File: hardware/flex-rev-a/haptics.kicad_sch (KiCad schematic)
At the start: 0 parts

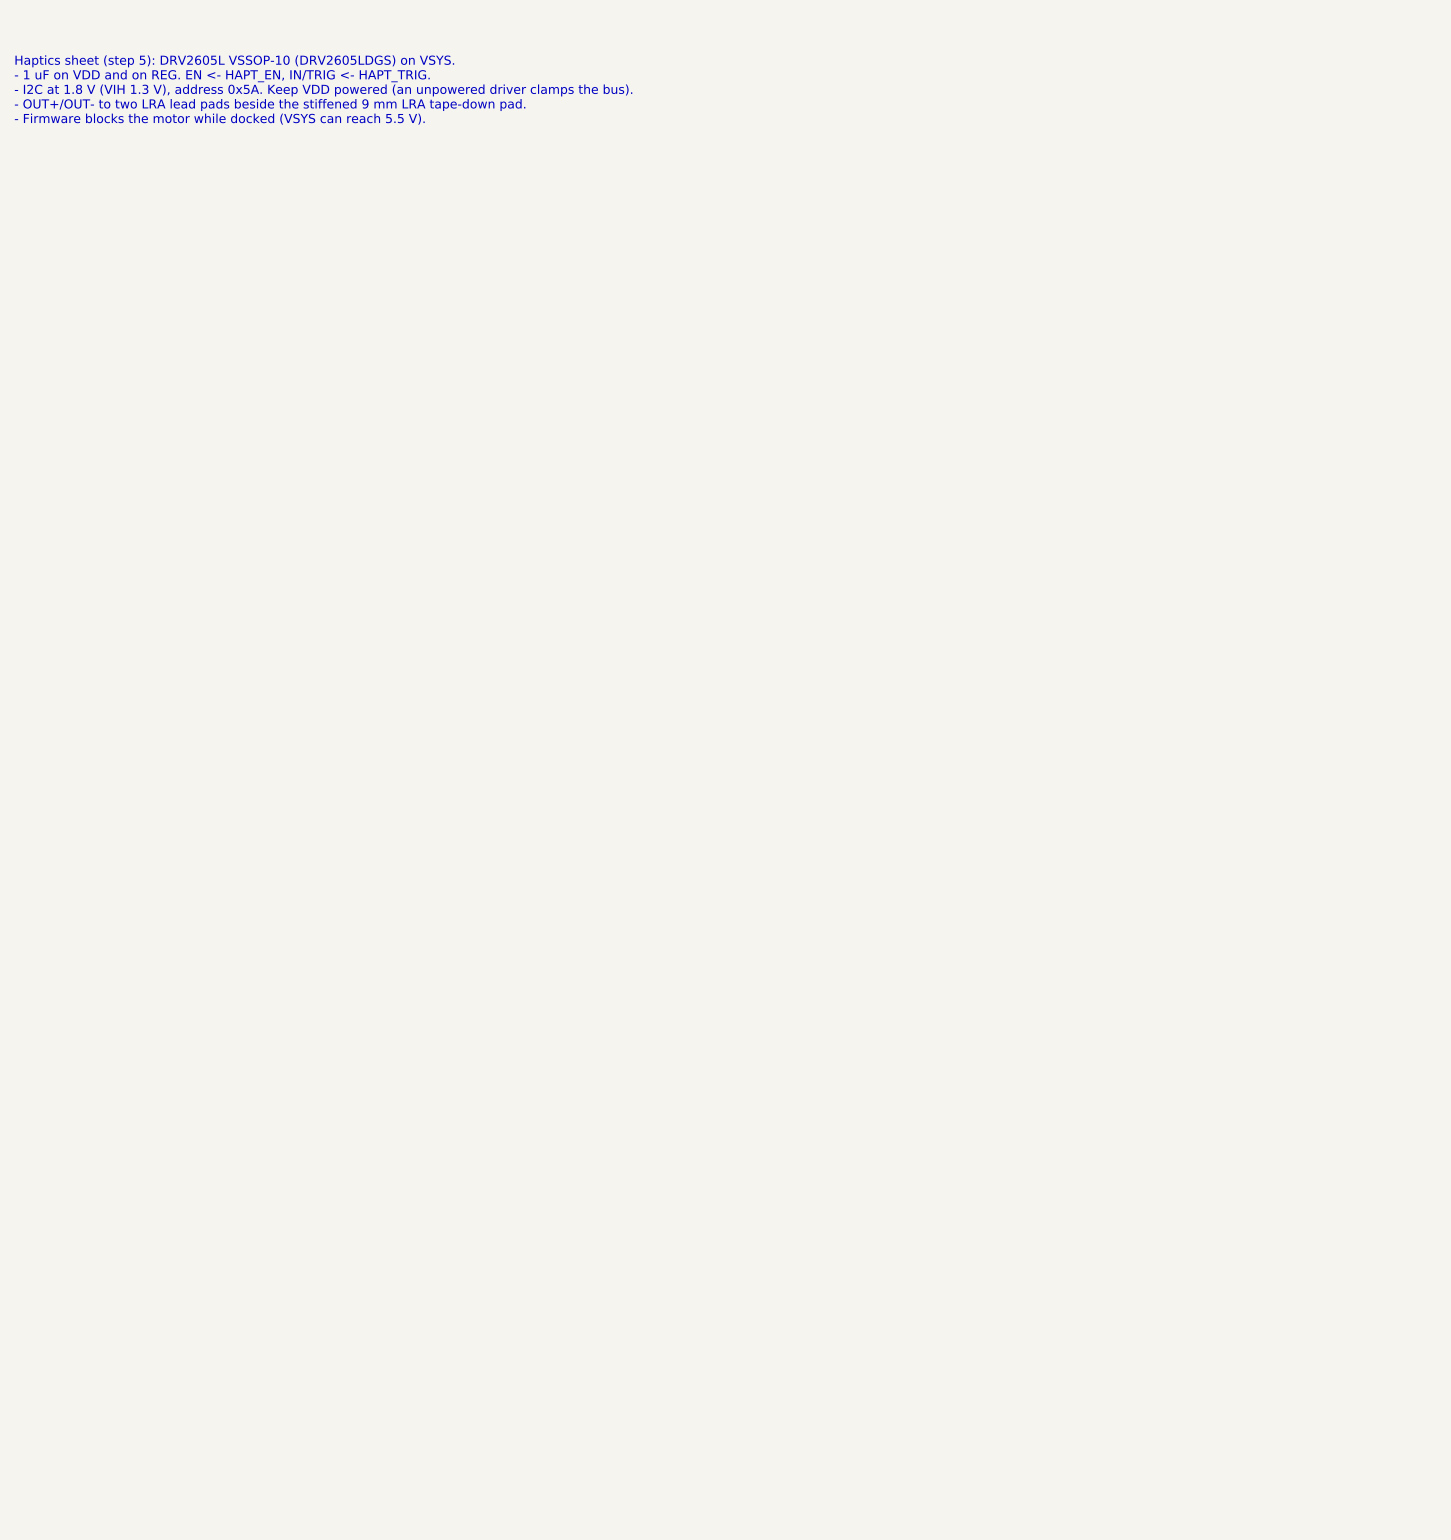
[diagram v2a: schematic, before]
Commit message: Draw haptics sheet: DRV2605L driving the coin LRA
From TI datasheet SLOS854D (DGS pin table):
- VDD (10) and VDD/NC (6) from VSYS with 1 uF; REG (1) with 1 uF.
- EN <- HAPT_EN, IN/TRIG <- HAPT_TRIG, SDA/SCL on the shared 1.8 V bus
  (VIH 1.3 V, address 0x5A).
- OUT+/OUT- to LRA lead pads TP501/TP502 (1.0 x 1.5 mm).
- Notes: the 9 mm LRA tape-down pad is a layout feature on an FR4
  stiffener; VDD must stay on (I2C pins limited to VDD + 0.3 V) and the
  motor is blocked while VBUS is present.

ERC: 2 errors, 7 warnings, none on the power, sensors or haptics sheets.

Co-Authored-By: Claude Opus 5.5 <noreply@anthropic.com>
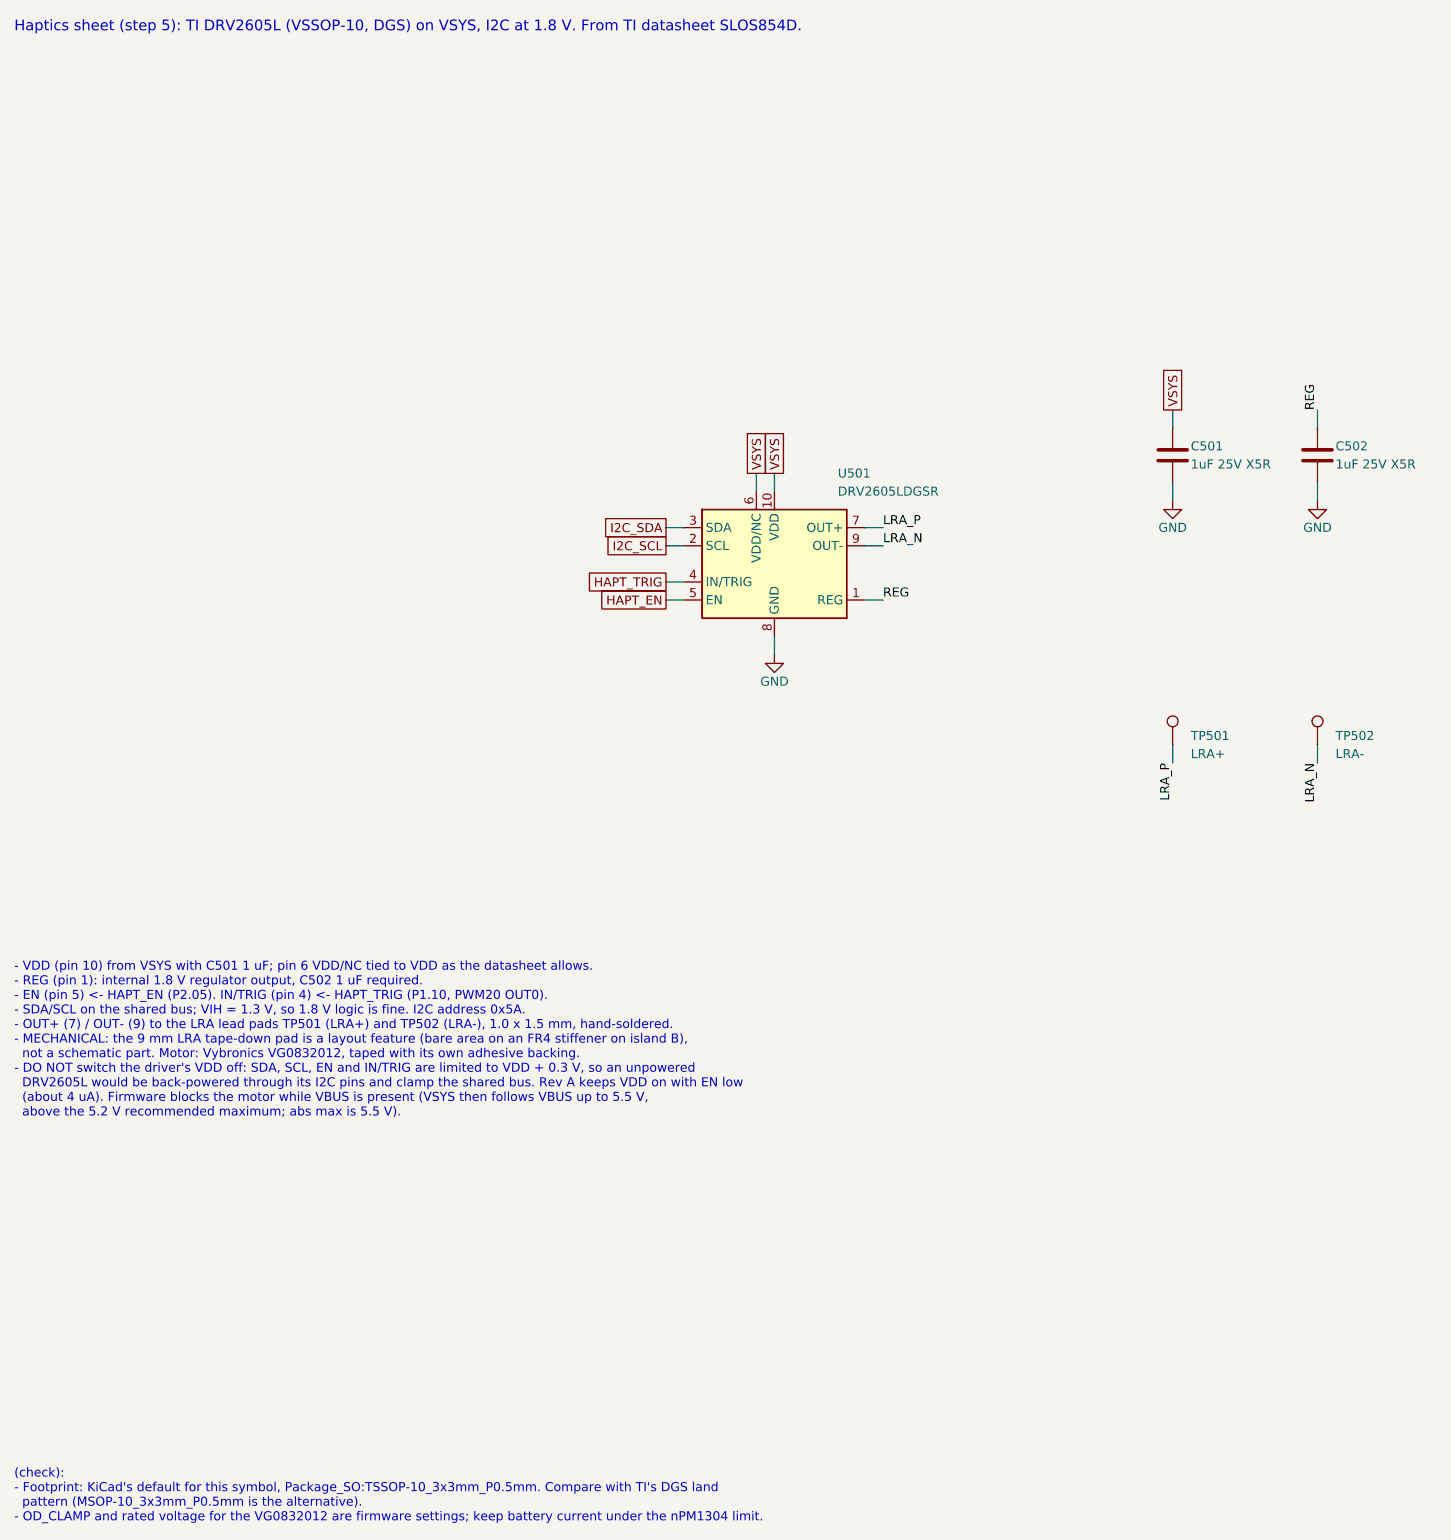
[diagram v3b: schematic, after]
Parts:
- added C501, C502: 1uF 25V X5R, Capacitor_SMD:C_0402_1005Metric, symbol Device:C
- added TP501: LRA+, wakeband:Pad_SMD_1.0x1.5mm, symbol Connector:TestPoint
- added TP502: LRA-, wakeband:Pad_SMD_1.0x1.5mm, symbol Connector:TestPoint
- added U501: DRV2605LDGSR, Package_SO:TSSOP-10_3x3mm_P0.5mm, symbol Driver:DRV2605LDGS
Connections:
- new net GND: C501.2, C502.2, U501.8 (GND)
- new net HAPT_EN: U501.5 (EN)
- new net HAPT_TRIG: U501.4 (IN/TRIG)
- new net I2C_SCL: U501.2 (SCL)
- new net I2C_SDA: U501.3 (SDA)
- new net LRA_N: TP502.1, U501.9 (OUT-)
- new net LRA_P: TP501.1, U501.7 (OUT+)
- new net REG: C502.1, U501.1 (REG)
- new net VSYS: C501.1, U501.10 (VDD), U501.6 (VDD/NC)
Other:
- note added: "(check): - Footprint: KiCad's default for this symbol, Package_SO:TSSOP-10_3x3mm_P0.5mm. Compare with TI's DGS land pattern (MSOP-10_3x3mm_P0.5mm is the alternative). - OD_CLAMP and rated voltage for the VG0832012 are firmware settings; keep battery current under the nPM1304 limit."
- note added: "- VDD (pin 10) from VSYS with C501 1 uF; pin 6 VDD/NC tied to VDD as the datasheet allows. - REG (pin 1): internal 1.8 V regulator output, C502 1 uF required. - EN (pin 5) <- HAPT_EN (P2.05). IN/TRIG (pin 4) <- HAPT_TRIG (P1.10, PWM20 OUT0). - SDA/SCL on the shared bus; VIH = 1.3 V, so 1.8 V logic is fine. I2C address 0x5A. - OUT+ (7) / OUT- (9) to the LRA lead pads TP501 (LRA+) and TP502 (LRA-),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"
- note added: "Haptics sheet (step 5): TI DRV2605L (VSSOP-10, DGS) on VSYS, I2C at 1.8 V. From TI datasheet SLOS854D."
- note removed: "Haptics sheet (step 5): DRV2605L VSSOP-10 (DRV2605LDGS) on VSYS. - 1 uF on VDD and on REG. EN <- HAPT_EN, IN/TRIG <- HAPT_TRIG. - I2C at 1.8 V (VIH 1.3 V), address 0x5A. Keep VDD powered (an unpowered driver clamps the bus). - OUT+/OUT- to two LRA lead pads beside the stiffened 9 mm LRA tape-down pad. - Firmware blocks the motor while docked (VSYS can reach 5.5 V)."

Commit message: Apply schematic review fixes: 2.0 V rail, pad 10 NC, VIN TVS, bulk cap
- Power: R202 47k -> 68k so BUCK1 starts at 2.0 V; global net VDD_1V8
  renamed VDD_2V0 on every sheet, notes updated.
- Haptics: DRV2605L IN/TRIG tied to GND, HAPT_TRIG removed (effects run
  over I2C). Footprint kept as Package_SO:TSSOP-10_3x3mm_P0.5mm: it is
  KiCad's TI DGS land pattern (cites MPDS035); KiCad 10 has no footprint
  named VSSOP-10_3x3mm_P0.5mm.
- MCU: pad 10 (P1.10) no-connect; GND global label replaced by the GND
  power symbol; note on the trapped lower-row GND pads 12/14/16/18 and on
  pads 8/24.
- Sensors: C403 10 uF on LIS2DW12 VDD per ST; related (check) removed.
- Dock: VIN TVS is now Littelfuse SMF18A (SOD-123FL, 18 V standoff, LCSC
  C409420); data pads keep TPD1E10B06, TPD1E0B04 noted as a lower-leakage
  alternative (check).
- bom.csv regenerated, PDF replotted, README updated.

ERC: 0 errors, 0 warnings.

Co-Authored-By: Claude Opus 5.5 <noreply@anthropic.com>
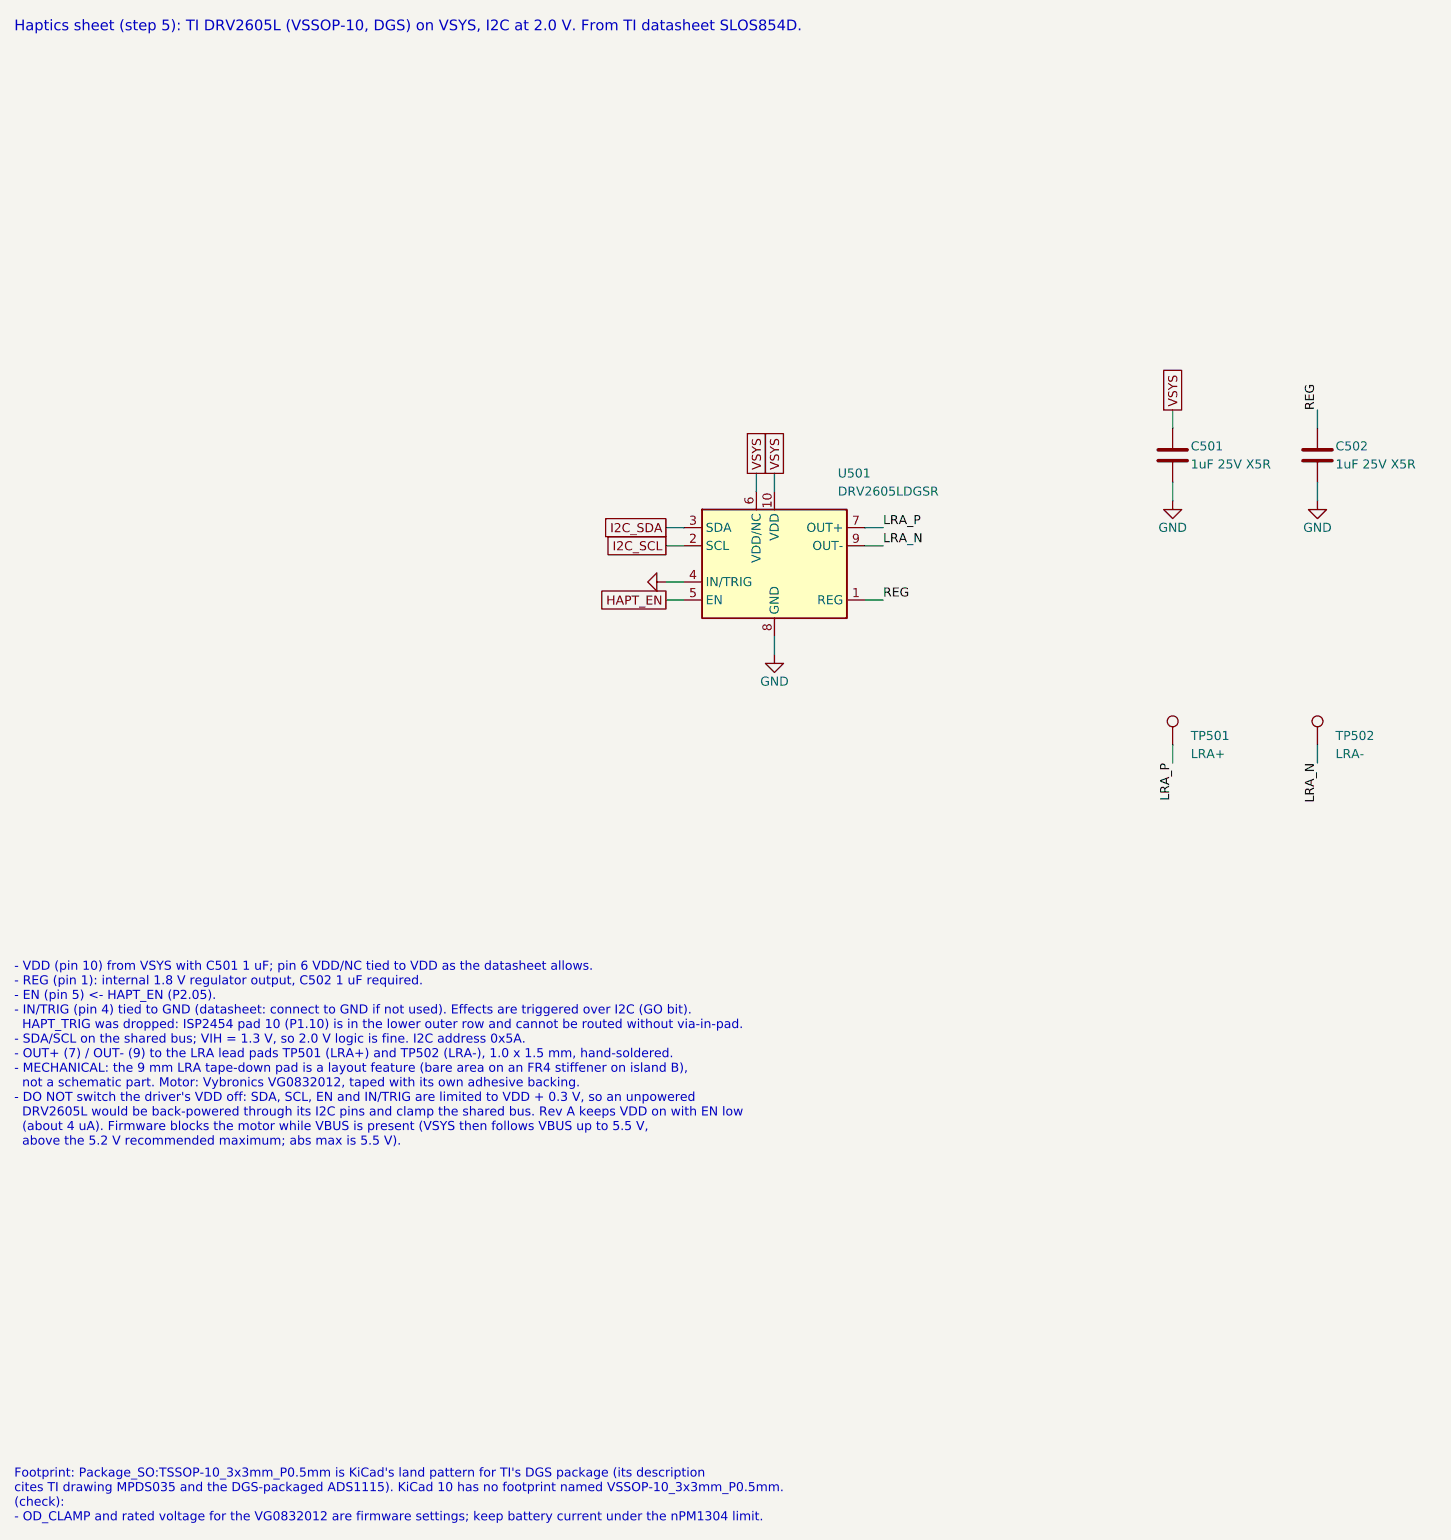
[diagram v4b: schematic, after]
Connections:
- net HAPT_TRIG is gone; now on net GND: U501.4 (IN/TRIG)
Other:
- note added: "- VDD (pin 10) from VSYS with C501 1 uF; pin 6 VDD/NC tied to VDD as the datasheet allows. - REG (pin 1): internal 1.8 V regulator output, C502 1 uF required. - EN (pin 5) <- HAPT_EN (P2.05). - IN/TRIG (pin 4) tied to GND (datasheet: connect to GND if not used). Effects are triggered over I2C (GO bit). HAPT_TRIG was dropped: ISP2454 pad 10 (P1.10) is in the lower outer row and cannot be routed wi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"
- note added: "Footprint: Package_SO:TSSOP-10_3x3mm_P0.5mm is KiCad's land pattern for TI's DGS package (its description cites TI drawing MPDS035 and the DGS-packaged ADS1115). KiCad 10 has no footprint named VSSOP-10_3x3mm_P0.5mm. (check): - OD_CLAMP and rated voltage for the VG0832012 are firmware settings; keep battery current under the nPM1304 limit."
- note added: "Haptics sheet (step 5): TI DRV2605L (VSSOP-10, DGS) on VSYS, I2C at 2.0 V. From TI datasheet SLOS854D."
- note removed: "(check): - Footprint: KiCad's default for this symbol, Package_SO:TSSOP-10_3x3mm_P0.5mm. Compare with TI's DGS land pattern (MSOP-10_3x3mm_P0.5mm is the alternative). - OD_CLAMP and rated voltage for the VG0832012 are firmware settings; keep battery current under the nPM1304 limit."
- note removed: "- VDD (pin 10) from VSYS with C501 1 uF; pin 6 VDD/NC tied to VDD as the datasheet allows. - REG (pin 1): internal 1.8 V regulator output, C502 1 uF required. - EN (pin 5) <- HAPT_EN (P2.05). IN/TRIG (pin 4) <- HAPT_TRIG (P1.10, PWM20 OUT0). - SDA/SCL on the shared bus; VIH = 1.3 V, so 1.8 V logic is fine. I2C address 0x5A. - OUT+ (7) / OUT- (9) to the LRA lead pads TP501 (LRA+) and TP502 (LRA-),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"
- note removed: "Haptics sheet (step 5): TI DRV2605L (VSSOP-10, DGS) on VSYS, I2C at 1.8 V. From TI datasheet SLOS854D."
